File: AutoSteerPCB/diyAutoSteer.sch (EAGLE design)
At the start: 65 parts, among them IC2 7805, IC3 7805, J1 I2C Out, J6 Reset, K4 CB1-P-12V, M1 ARDUINO-NANO-3.0, U2 ADC-4CH-ADS1115

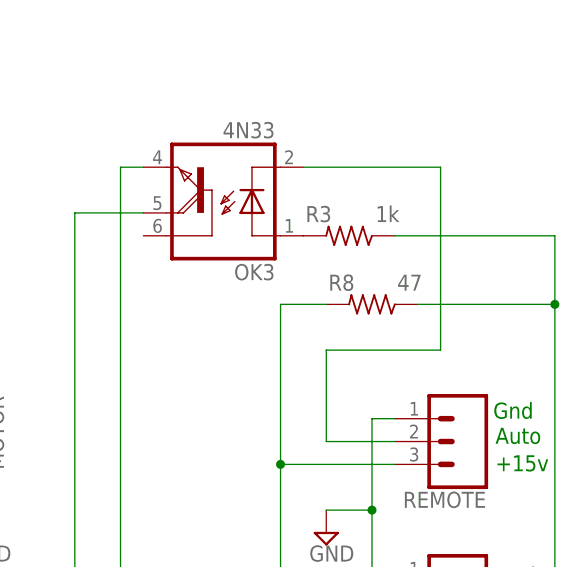
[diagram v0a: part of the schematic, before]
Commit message: Added ADS1115 to parts
Missed part, change R8 to zero ohms
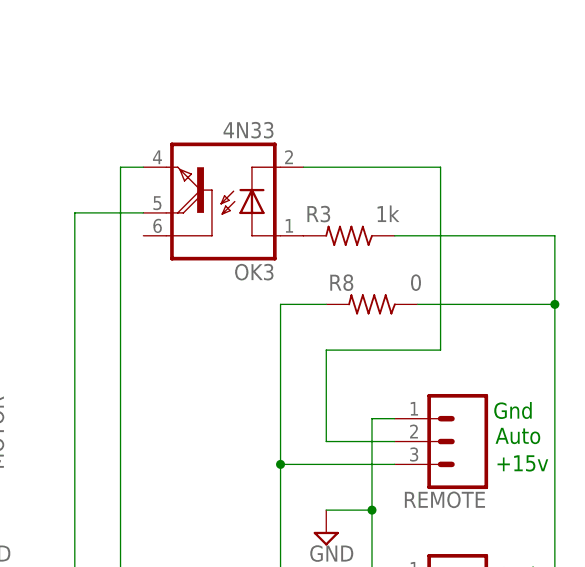
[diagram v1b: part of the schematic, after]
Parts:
- R8: value 47 -> 0
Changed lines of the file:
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@@
 <part name="IMP" library="SparkFun-Connectors" deviceset="CONN_03" device="LONGPADS"/>
 <part name="STEER" library="SparkFun-Connectors" deviceset="CONN_03" device="LONGPADS"/>
-<part name="R8" library="rcl" deviceset="R-US_" device="0309/12" value="47"/>
+<part name="R8" library="rcl" deviceset="R-US_" device="0309/12" value="0"/>
 </parts>
 <sheets>

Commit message: v2 PCB
v2 PCB
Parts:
- removed 12S5: WIREPAD3,81/1,1, wirepad:WIREPAD3,81/1,1
- removed A1: A2, SparkFun-Connectors:CONN_02PTH3
- removed D5, INT0: (no value), SparkFun-Connectors:CONN_01PTH_LONGPAD
- added +5V_OUT, ANALOGIN: (no value), SparkFun-Connectors:CONN_03LONGPADS
- added J2: Pins, SparkFun-Connectors:CONN_02PTH3
- D2: value 1N4004 -> 3A diode; device diode:1N4004 -> diode:DIODE-DO27-15
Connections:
- removed net N$9: D5.1, M1.D5
- new net N$14: ANALOGIN.2, M1.A1
- new net N$18: J2.1, M1.D5
- net +5V: now also +5V_OUT.1, +5V_OUT.2, +5V_OUT.3
- net BATT: now also K41.1; no longer K41.2
- net N$10: now also ANALOGIN.3, M1.A0; no longer A1.1, M1.A2
- net N$15: now also ANALOGIN.1, M1.A2; no longer A1.2, M1.A1
- net N$24: now also K41.2; no longer K41.1
- net N$6: now also J2.2; no longer INT0.1
- net SW_RAW: no longer 12S5.P
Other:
- moved on the sheet: GN1, GN4, K4

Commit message: Version 2
Version 2 of PCB
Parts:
- added +12V, DOG2: (no value), SparkFun-Connectors:CONN_02PTH3
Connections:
- net +15V: now also +12V.1, +12V.2, DOG2.1
- net GND: now also DOG2.2
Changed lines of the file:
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@@
 <part name="GN1" library="wirepad" deviceset="WIREPAD" device="3,81/1,1"/>
 <part name="GN4" library="wirepad" deviceset="WIREPAD" device="3,81/1,1"/>
+<part name="+12V" library="SparkFun-Connectors" deviceset="CONN_02" device="PTH3"/>
+<part name="DOG2" library="SparkFun-Connectors" deviceset="CONN_02" device="PTH3"/>
 </parts>
 <sheets>
@@
 <attribute name="NAME" x="108.5342" y="180.721" size="1.778" layer="95" rot="R270"/>
 </instance>
+<instance part="+12V" gate="G$1" x="101.6" y="152.4" rot="R180"/>
+<instance part="DOG2" gate="G$1" x="45.72" y="142.24"/>
 </instances>
 <busses>
@@
 <wire x1="66.04" y1="152.4" x2="66.04" y2="149.86" width="0.1524" layer="91"/>
 <pinref part="D1" gate="1" pin="A"/>
+<pinref part="DOG2" gate="G$1" pin="2"/>
+<wire x1="53.34" y1="144.78" x2="53.34" y2="149.86" width="0.1524" layer="91"/>
+<wire x1="53.34" y1="149.86" x2="66.04" y2="149.86" width="0.1524" layer="91"/>
+<junction x="66.04" y="149.86"/>
 </segment>
 <segment>
@@
 <pinref part="C20" gate="G$1" pin="+"/>
 <pinref part="D2" gate="G$1" pin="C"/>
-</segment>
-</net>
+<wire x1="86.36" y1="162.56" x2="93.98" y2="162.56" width="0.1524" layer="91"/>
+<junction x="86.36" y="162.56"/>
+<pinref part="+12V" gate="G$1" pin="1"/>
+<wire x1="93.98" y1="162.56" x2="93.98" y2="152.4" width="0.1524" layer="91"/>
+<pinref part="+12V" gate="G$1" pin="2"/>
+<wire x1="93.98" y1="152.4" x2="93.98" y2="149.86" width="0.1524" layer="91"/>
+<junction x="93.98" y="152.4"/>
+<pinref part="DOG2" gate="G$1" pin="1"/>
+<wire x1="53.34" y1="142.24" x2="53.34" y2="137.16" width="0.1524" layer="91"/>
+<wire x1="53.34" y1="137.16" x2="71.12" y2="137.16" width="0.1524" layer="91"/>
+</segment>
+</net>
